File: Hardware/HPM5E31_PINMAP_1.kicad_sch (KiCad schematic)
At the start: 4 parts

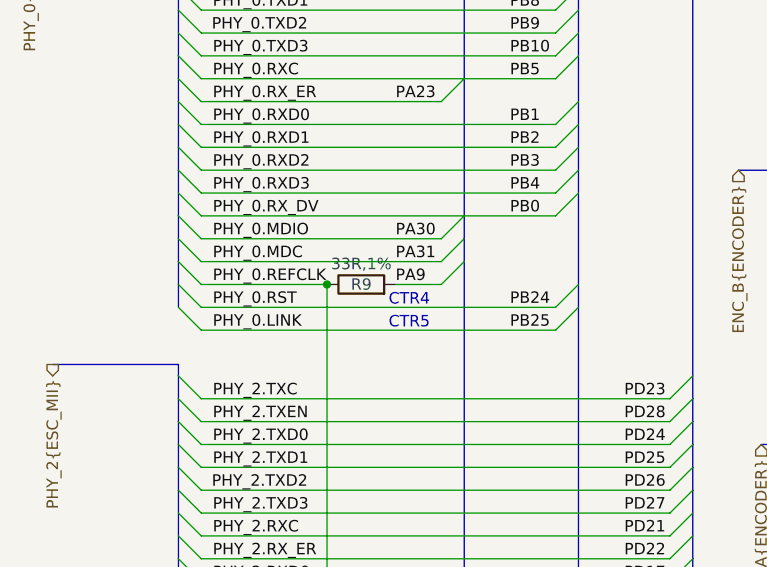
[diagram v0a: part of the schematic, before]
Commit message: PCB：网口替换为HR911205C
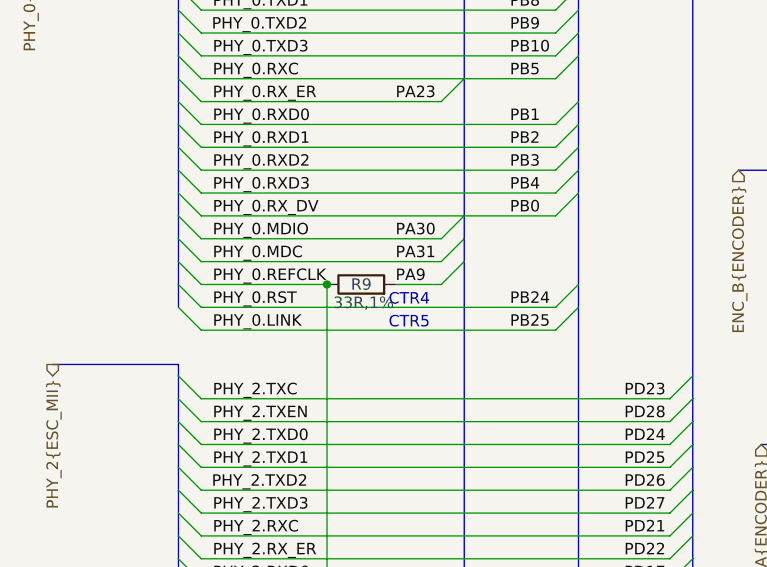
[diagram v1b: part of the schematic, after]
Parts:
- R9: footprint Resistor_SMD:R_0402_1005Metric -> Resistor_SMD:R_0201_0603Metric; symbol HPM6280Foc:0402WGF330JTCE -> HPM6280Foc:RC0201FR-0733RL; 立创编号 C25105 -> C295794
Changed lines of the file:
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@@
 	)
 	(symbol
-		(lib_id "HPM6280Foc:0402WGF330JTCE")
+		(lib_id "HPM6280Foc:RC0201FR-0733RL")
 		(at 60.96 62.23 0)
 		(unit 1)
@@
 		)
 		(property "Value" "33R,1%"
-			(at 60.96 59.944 0)
+			(at 61.214 64.262 0)
 			(effects
 				(font
@@
 			)
 		)
-		(property "Footprint" "Resistor_SMD:R_0402_1005Metric"
+		(property "Footprint" "Resistor_SMD:R_0201_0603Metric"
 			(at 60.96 62.23 0)
 			(effects
@@
 			)
 		)
-		(property "Datasheet" ""
+		(property "Datasheet" "https://item.szlcsc.com/datasheet/RC0201FR-0733RL/280211.html?spm=sc.it.xds.a___sc.cidn.xh1.zy.n&lcsc_vid=QwNcXlxQFQcLXlxWEwBbBlMDTgAMBAZTEwNcU1EARVkxVlNTTlVZUVdTQVNXVDtW"
 			(at 60.96 62.23 0)
 			(effects
@@
 			)
 		)
-		(property "Description" ""
+		(property "Description" "厚膜电阻 33Ω ±1% 50mW"
 			(at 60.96 62.23 0)
 			(effects
@@
 			)
 		)
-		(property "立创编号" "C25105"
+		(property "立创编号" "C295794"
 			(at 60.96 62.23 0)
 			(effects
